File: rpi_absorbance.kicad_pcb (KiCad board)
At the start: 2 copper layers, 13 parts, among them P1 CONN_01X05, U1 MAX6071, U2 LTC2452, U3 SD100-13-23-222, U4 OPA381

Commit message: Improve PCB layout
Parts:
- added C8: 10u, Capacitors_SMD:C_0603, F.Cu at (136.6, 103.8)
- added R2: 16k, Resistors_SMD:R_0603, F.Cu at (135.3, 101.8)
- C1, C2, C3, C4, C5, C6, C7: footprint Capacitors_SMD:C_0603_HandSoldering -> Capacitors_SMD:C_0603
- R1: footprint Resistors_SMD:R_0603_HandSoldering -> Resistors_SMD:R_0603
- moved C1 22.8 mm to (125.9, 95.9)
- moved U1 21.7 mm to (130.8, 97.4)
- moved C7 15.7 mm to (129.9, 105.7), turned to 270 degrees
- moved R1 14.3 mm to (131.4, 105.7), turned to 270 degrees
- moved C6 10.9 mm to (132.7, 100.4), turned to 180 degrees
- moved U2 7.83 mm to (138.1, 98.2)
- moved C5 6.22 mm to (140.0, 107.0)
- moved C4 1.21 mm to (132.7, 101.8)
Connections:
- U2 pad 6: Net-(C7-Pad1) -> Net-(C8-Pad1)
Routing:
- net GND: track 2.88 -> 11.5 mm
- net Net-(C7-Pad1): track 0.00 -> 7.42 mm
- net Net-(C7-Pad2): track 3.39 -> 8.40 mm
- net Net-(C8-Pad1): track 0.00 -> 4.61 mm
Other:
- rule pad_to_mask_clearance: 0.2 -> 0.0508

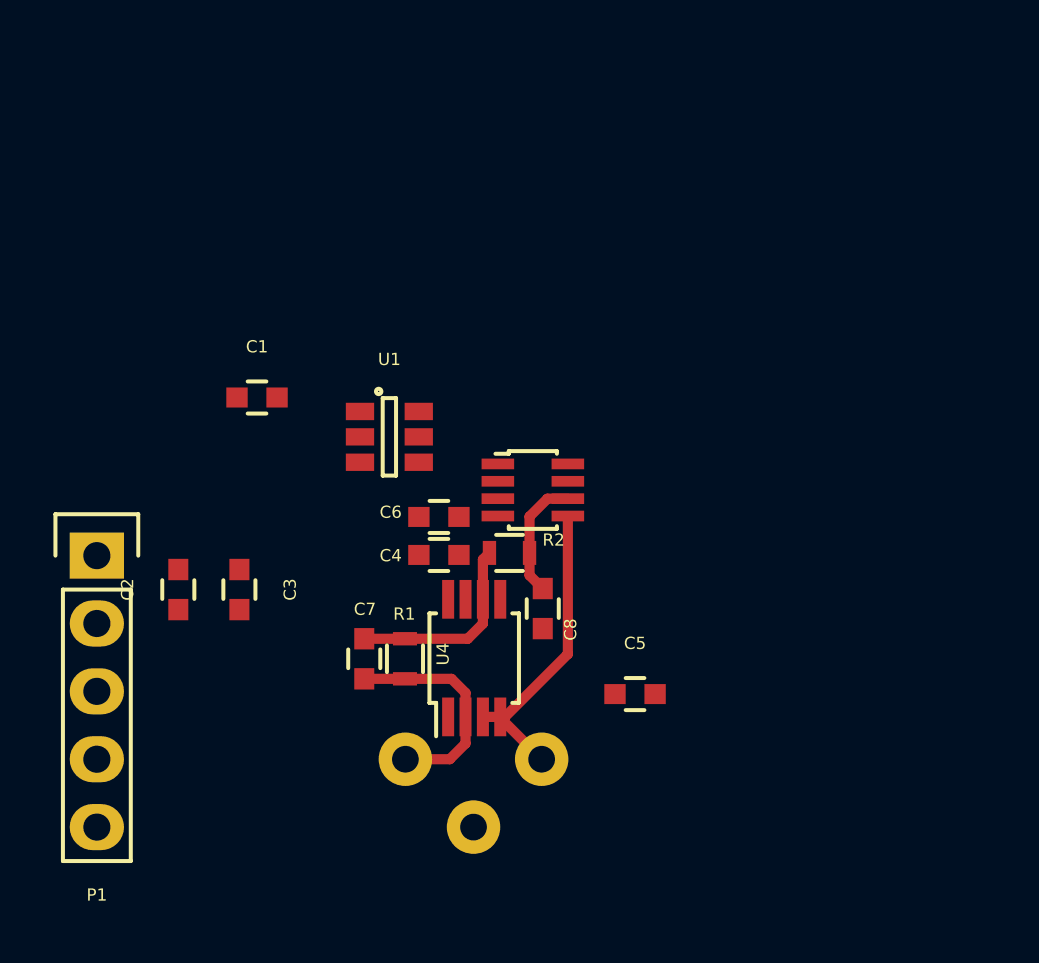
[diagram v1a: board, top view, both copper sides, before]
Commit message: Add different ADC
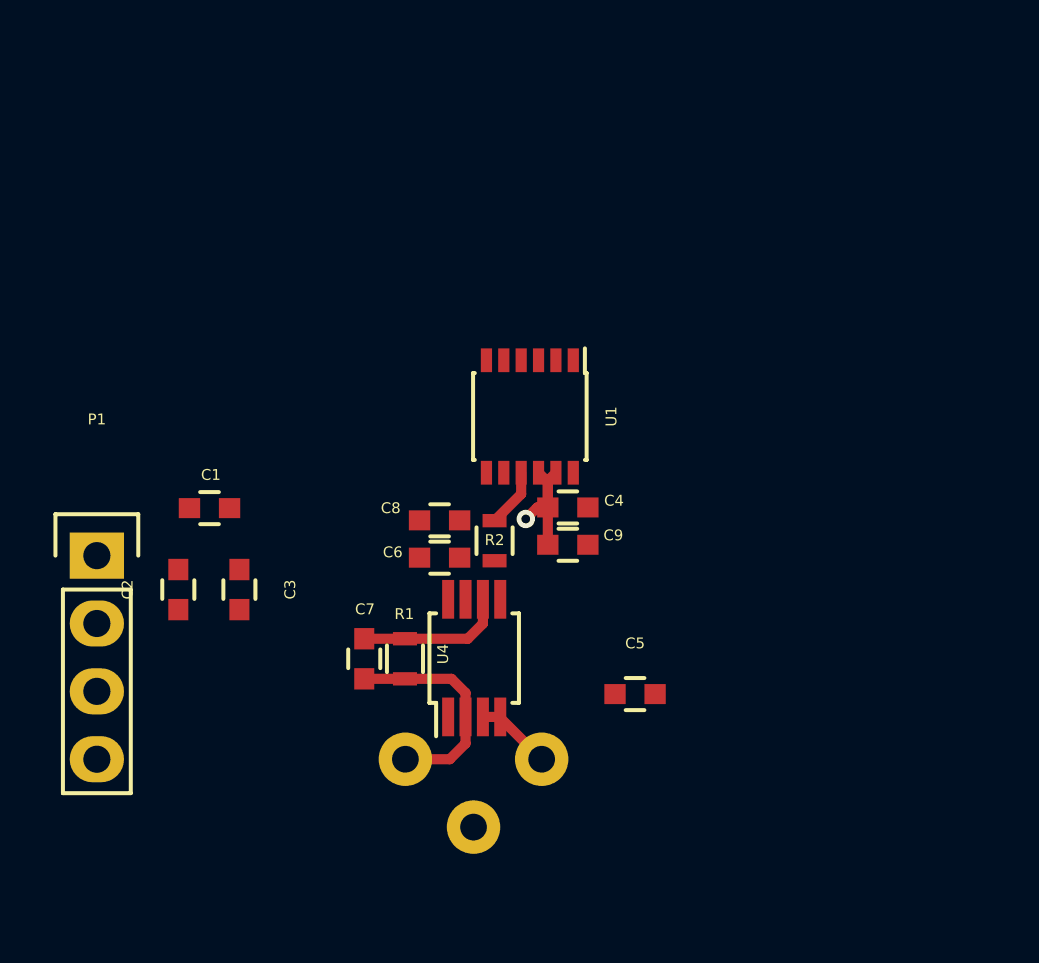
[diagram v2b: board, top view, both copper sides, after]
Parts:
- removed U2: LTC2452, footprints:TSOT-23-8
- added C9: 10u, Capacitors_SMD:C_0603, F.Cu at (137.5, 101.4)
- P1: value CONN_01X05 -> CONN_01X04; footprint Pin_Headers:Pin_Header_Straight_1x05 -> Pin_Headers:Pin_Header_Straight_1x04
- U1: value MAX6071 -> LTC2461; footprint TO_SOT_Packages_SMD:SOT-23-6 -> Housings_SSOP:MSOP-12_3x4mm_Pitch0.65mm
- moved U1 5.31 mm to (136.1, 96.6), turned to 270 degrees
- moved C4 5.14 mm to (137.5, 100.1)
- moved C8 5.08 mm to (132.7, 100.5), turned to 180 degrees
- moved C1 4.51 mm to (124.1, 100.1)
- moved C6 1.52 mm to (132.7, 101.9)
- moved R2 0.72 mm to (134.8, 101.3), turned to 90 degrees
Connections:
- C1 pad 1: GND -> Net-(C1-Pad1)
- C1 pad 2: Net-(C1-Pad2) -> GND
- C2 pad 1: VCC -> Net-(C2-Pad1)
- P1 pad 3: Net-(P1-Pad3) -> /SDA
- P1 pad 4: Net-(P1-Pad4) -> /SCL
- U1 pad 1: GND -> Net-(C1-Pad1)
- U1 pad 2: GND -> Net-(C2-Pad1)
- U1 pad 3: VCC -> GND
- U1 pad 4: VCC -> GND
- U1 pad 5: Net-(C1-Pad2) -> /SCL
- U1 pad 6: Net-(C1-Pad2) -> /SDA
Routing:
- net GND: track 11.5 -> 8.14 mm, vias 0 -> 1
- net Net-(C8-Pad1): track 4.61 -> 2.21 mm
- net Net-(C7-Pad1): track 7.42 -> 5.58 mm
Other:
- rule pad_to_mask_clearance: 0.0508 -> 0.0254

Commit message: Rearrange components
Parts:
- moved P1 24.7 mm to (138.6, 85.7), turned to 270 degrees
- moved C5 19.3 mm to (137.5, 87.9)
- moved C3 18.5 mm to (137.6, 89.3), turned to 0 degrees
- moved C2 17.3 mm to (136.7, 92.6)
- moved C1 15.9 mm to (138.1, 92.6), turned to 90 degrees
- moved C7 8.15 mm to (138.0, 105.7)
- moved R1 5.14 mm to (136.6, 105.7)
- moved C9 3.70 mm to (139.0, 98.1), turned to 270 degrees
- moved C4 0.48 mm to (138.0, 100.0)
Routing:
- net GND: track 8.14 -> 17.4 mm, vias 1 -> 7
- net Net-(C2-Pad1): track 0.00 -> 1.36 mm
- net Net-(C1-Pad1): track 0.00 -> 1.36 mm
- net Net-(C8-Pad1): track 2.21 -> 3.52 mm
- net Net-(C7-Pad1): track 5.58 -> 6.55 mm
- net Net-(C7-Pad2): track 8.40 -> 8.96 mm

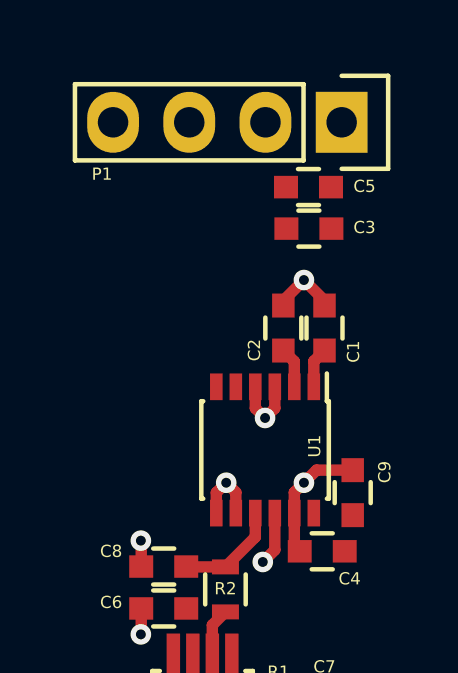
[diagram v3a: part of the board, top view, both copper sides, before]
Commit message: Reorganize PCB
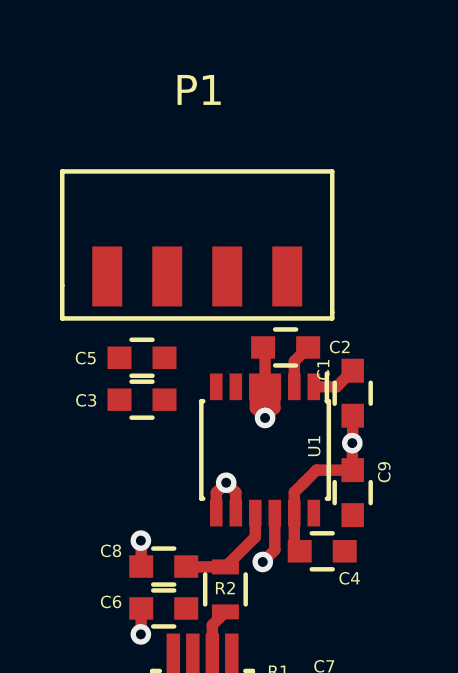
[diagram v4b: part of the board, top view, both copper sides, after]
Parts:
- P1: footprint Pin_Headers:Pin_Header_Straight_1x04 -> footprints:CONN_1x4_SMT_2mm
- moved C3 7.97 mm to (132.0, 95.0), turned to 180 degrees
- moved C5 7.95 mm to (132.0, 93.6), turned to 180 degrees
- moved P1 4.89 mm to (133.8, 86.6), turned to 0 degrees
- moved C1 2.37 mm to (139.0, 94.8), turned to 270 degrees
- moved C2 0.65 mm to (136.8, 93.2), turned to 180 degrees
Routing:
- net GND: track 17.4 -> 19.3 mm, vias 7 -> 6

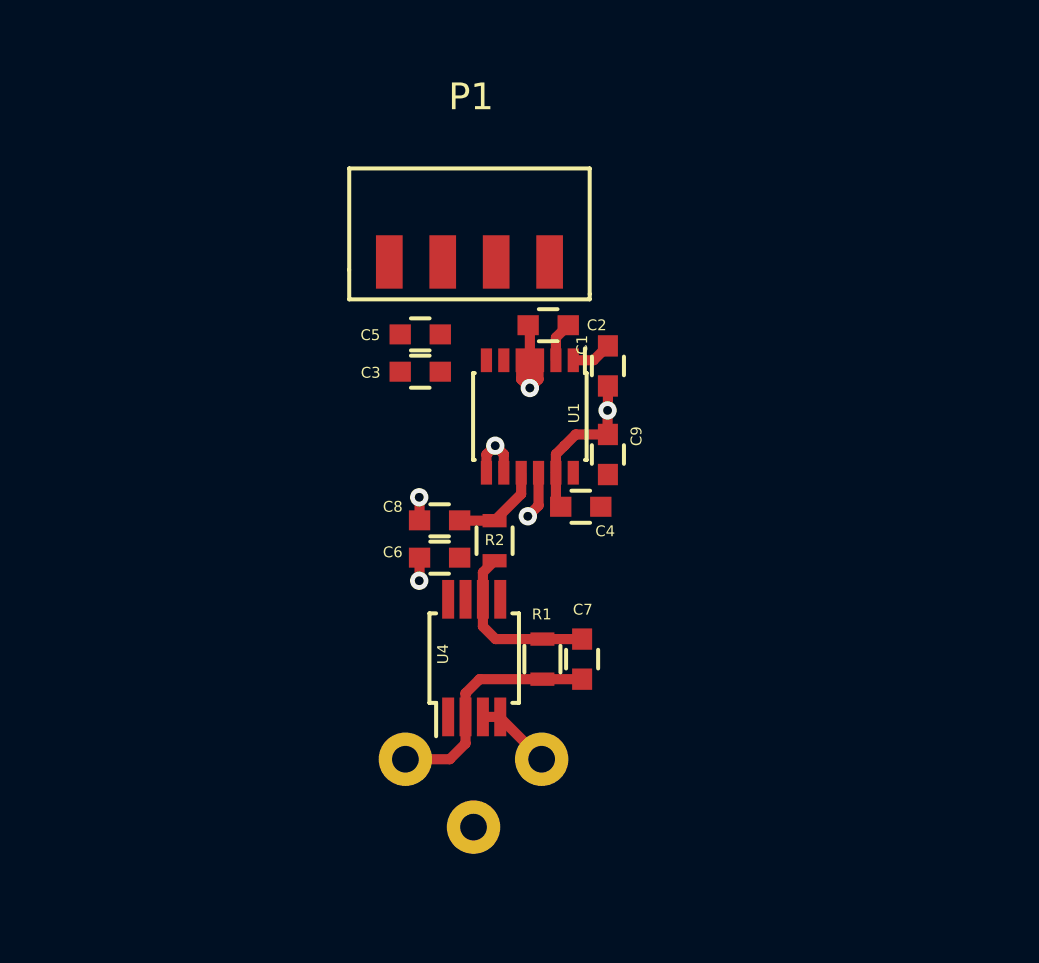
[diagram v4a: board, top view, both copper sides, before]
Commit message: Add USB AB micro connector
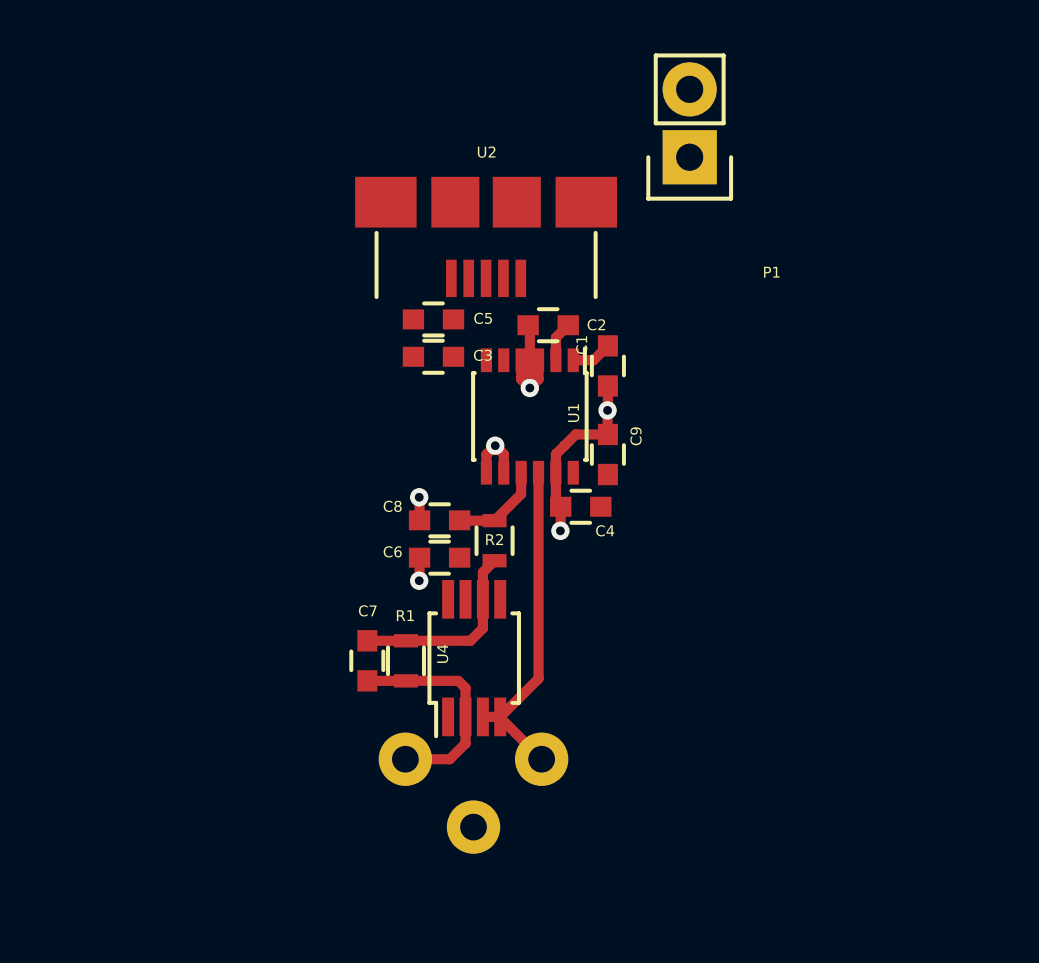
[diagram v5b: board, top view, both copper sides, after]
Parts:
- added U2: RPIABS_CONN, footprints:FCI_10104111-0001LF, F.Cu at (134.5, 92.2)
- P1: value CONN_01X04 -> CONN_01X02; footprint footprints:CONN_1x4_SMT_2mm -> Pin_Headers:Pin_Header_Straight_1x02
- moved P1 8.25 mm to (142.1, 86.9), turned to 180 degrees
- moved C7 8.04 mm to (130.0, 105.8)
- moved R1 5.11 mm to (131.5, 105.8)
- moved C3 0.75 mm to (132.5, 94.4), turned to 0 degrees
- moved C5 0.75 mm to (132.5, 93.0), turned to 0 degrees
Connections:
- P1 pad 2: VCC -> Net-(P1-Pad2)
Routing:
- net GND: track 19.3 -> 28.1 mm
- net Net-(C7-Pad1): track 6.55 -> 7.23 mm
- net Net-(C7-Pad2): track 8.96 -> 8.35 mm

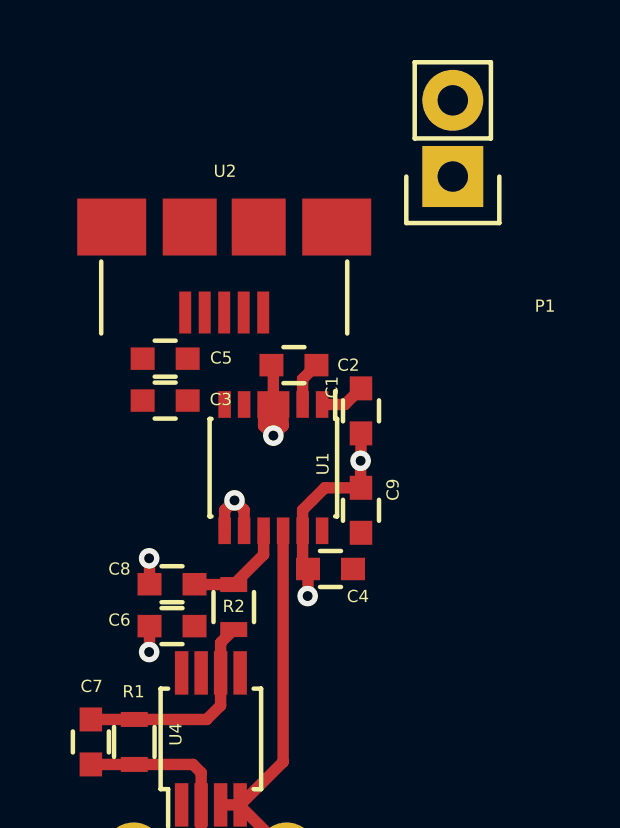
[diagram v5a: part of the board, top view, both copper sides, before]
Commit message: Reorganize PCB
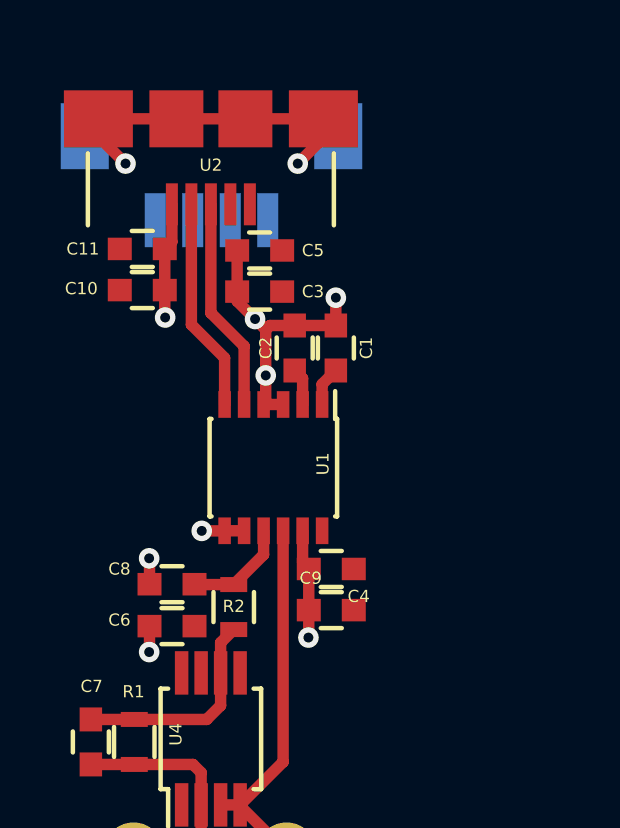
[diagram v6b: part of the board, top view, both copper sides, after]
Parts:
- added C10: 1u, Capacitors_SMD:C_0603, F.Cu at (131.7, 90.7)
- added C11: .1u, Capacitors_SMD:C_0603, F.Cu at (131.7, 89.4)
- C3, C9: value 10u -> 1u
- C5: value 1u -> .1u
- P1: value CONN_01X02 -> CONN_01X04; footprint Pin_Headers:Pin_Header_Straight_1x02 -> footprints:Hirose_DF13-4P-1.25V(20); moved to B.Cu
- moved P1 10.5 mm to (132.2, 90.4), turned to 0 degrees
- moved C3 4.81 mm to (135.6, 90.8)
- moved C5 4.79 mm to (135.6, 89.4)
- moved U2 3.63 mm to (134.0, 88.6)
- moved C9 3.47 mm to (138.0, 101.4), turned to 0 degrees
- moved C1 2.26 mm to (138.2, 92.7), turned to 90 degrees
- moved C2 0.57 mm to (136.8, 92.7), turned to 90 degrees
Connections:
- P1 pad 2: Net-(P1-Pad2) -> VCC
- U2 pad 1: Net-(P1-Pad2) -> VCC
- U2 pad 2: /SCL -> Net-(U2-Pad2)
- U2 pad 3: /SDA -> /SCL
- U2 pad 4: VCC -> /SDA
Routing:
- net GND: track 28.1 -> 44.8 mm, vias 6 -> 10
- net /SDA: track 0.00 -> 7.13 mm
- net /SCL: track 0.00 -> 7.13 mm

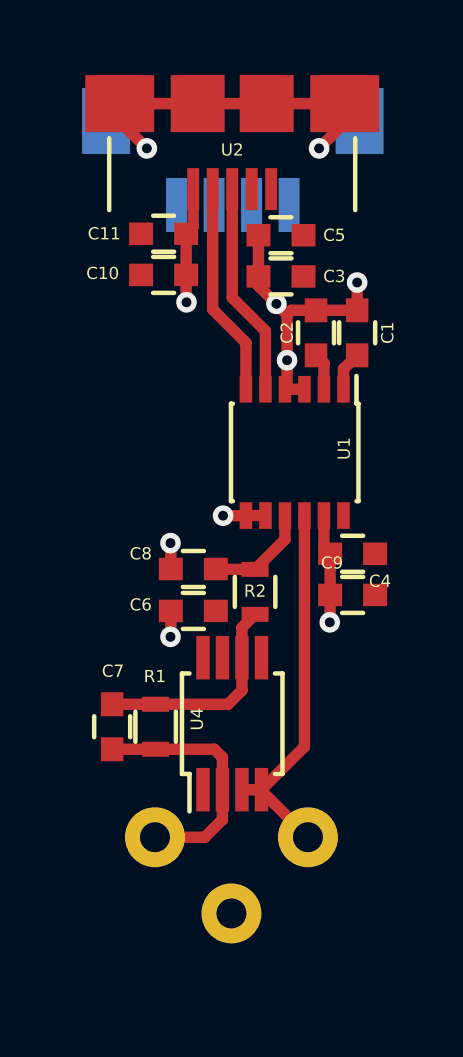
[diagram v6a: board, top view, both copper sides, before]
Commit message: Add power planes
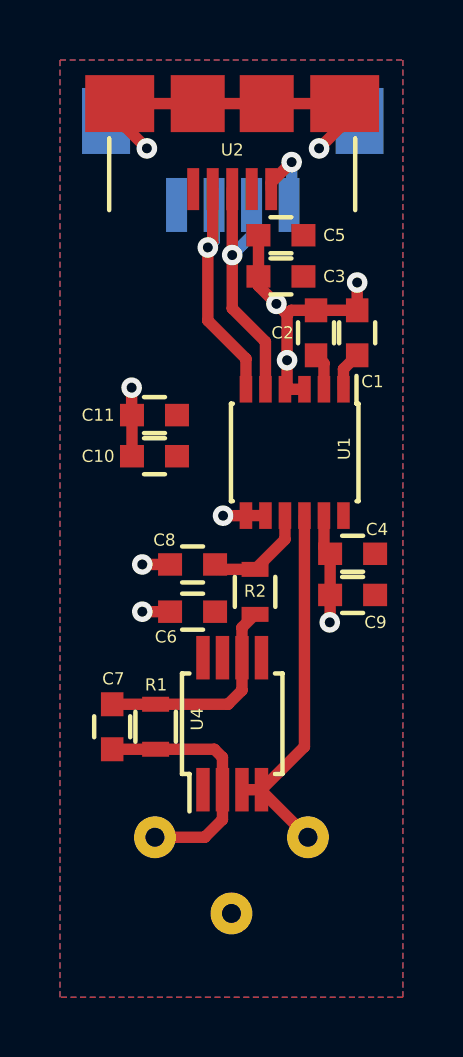
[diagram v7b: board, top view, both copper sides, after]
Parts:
- moved C10 6.05 mm to (131.4, 96.8), turned to 0 degrees
- moved C11 6.05 mm to (131.4, 95.4), turned to 0 degrees
- moved C8 0.15 mm to (132.7, 100.4)
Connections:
- P1 pad 2: VCC -> /SDA
- P1 pad 3: Net-(P1-Pad3) -> /SCL
- P1 pad 4: Net-(P1-Pad4) -> VCC
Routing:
- net VCC: track 0.00 -> 2.65 mm, vias 0 -> 1
- net /SCL: track 7.13 -> 9.07 mm, vias 0 -> 1
- net /SDA: track 7.13 -> 8.77 mm, vias 0 -> 1
- net GND: track 44.8 -> 43.3 mm
- added copper zone on B.Cu, net GND
- added copper zone on F.Cu, net VCC

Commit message: Make final adjustments
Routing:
- net GND: track 43.3 -> 45.1 mm, vias 10 -> 11
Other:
- board outline added: 11.7 x 31.5 mm
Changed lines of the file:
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@@
   (general
     (links 49)
-    (no_connects 1)
-    (area 128.27 83.392399 139.700001 114.808001)
+    (no_connects 0)
+    (area 128.067999 83.363999 139.902001 115.010001)
     (thickness 1.6)
-    (drawings 0)
-    (tracks 90)
+    (drawings 4)
+    (tracks 93)
     (zones 0)
     (modules 18)
@@
     (visible_elements FFFFF77F)
     (pcbplotparams
-      (layerselection 0x00030_80000001)
+      (layerselection 0x010f0_80000001)
       (usegerberextensions false)
       (excludeedgelayer true)
@@
       (outputformat 1)
       (mirror false)
-      (drillshape 1)
+      (drillshape 0)
       (scaleselection 1)
-      (outputdirectory ""))
+      (outputdirectory gerber/))
   )
   (net 0 "")
@@
     (tags "SSOP 0.65")
     (attr smd)
-    (fp_text reference U4 (at 0.1524 -1.1684 270) (layer F.SilkS)
+    (fp_text reference U4 (at 0.0254 -0.0254 360) (layer F.SilkS)
       (effects (font (size 0.4064 0.4064) (thickness 0.08128)))
     )
@@
     (tags "resistor 0603")
     (attr smd)
-    (fp_text reference R2 (at 0.0254 0 180) (layer F.SilkS)
+    (fp_text reference R2 (at 1.4732 -0.0254 180) (layer F.SilkS)
       (effects (font (size 0.4064 0.4064) (thickness 0.08128)))
     )
@@
     (tags "SSOP 0.65")
     (attr smd)
-    (fp_text reference U1 (at -0.127 -1.651 270) (layer F.SilkS)
-      (effects (font (size 0.4064 0.4064) (thickness 0.08128)))
-    )
-    (fp_text value LTC2461 (at -0.2032 0.1016 360) (layer F.Fab)
+    (fp_text reference U1 (at 0.127 -0.0508 360) (layer F.SilkS)
+      (effects (font (size 0.4064 0.4064) (thickness 0.08128)))
+    )
+    (fp_text value LTC2461 (at -0.889 -0.0508 360) (layer F.Fab)
       (effects (font (size 0.4064 0.4064) (thickness 0.08128)))
     )
@@
   (module "footprints:Hirose_DF13-4P-1.25V(20)" (layer B.Cu)
     (at 132.1562 90.3986)
-    (fp_text reference P1 (at -1.6002 -0.3302) (layer B.SilkS)
+    (fp_text reference P1 (at 1.8542 -3.8354) (layer B.SilkS)
       (effects (font (size 0.4064 0.4064) (thickness 0.08128)) (justify mirror))
     )
@@
       (net 7 "Net-(C7-Pad2)"))
   )
+  (gr_line (start 139.827 114.935) (end 139.827 83.439) (angle 90) (layer Edge.Cuts) (width 0.15))
+  (gr_line (start 128.143 114.935) (end 139.827 114.935) (angle 90) (layer Edge.Cuts) (width 0.15))
+  (gr_line (start 128.143 83.439) (end 128.143 114.935) (angle 90) (layer Edge.Cuts) (width 0.15))
+  (gr_line (start 139.827 83.439) (end 128.143 83.439) (angle 90) (layer Edge.Cuts) (width 0.15))
+  (segment (start 132.7104 87.8698) (end 132.1958 87.8698) (width 0.381) (layer F.Cu) (net 1))
+  (via (at 131.2672 88.7984) (size 0.6858) (drill 0.3302) (layers F.Cu B.Cu) (net 1))
+  (segment (start 132.1958 87.8698) (end 131.2672 88.7984) (width 0.381) (layer F.Cu) (net 1))
   (segment (start 131.9396 101.9556) (end 131.0132 101.9556) (width 0.381) (layer F.Cu) (net 1))
   (via (at 131.0132 101.9556) (size 0.6858) (drill 0.3302) (layers F.Cu B.Cu) (net 1))
